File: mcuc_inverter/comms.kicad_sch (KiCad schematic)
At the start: 0 parts

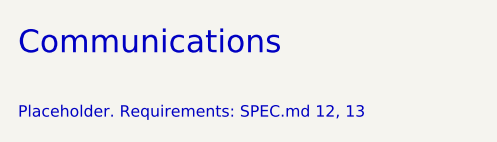
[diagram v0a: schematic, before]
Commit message: Design the supervisor interlock block
Adds docs/supervisor.md: the full logic design for the firmware-independent
hardware interlocks required by SPEC.md §9.2 -- overcurrent detect and latch,
fault aggregation, PWM overlap elimination and dead time. Includes the
24-signal interface, gate budget, and a failure-mode review done on the
assumption that firmware is hostile.

Two selections differ from the original PALTA board, both deliberate:

- Comparators run from +5 V, not 3.3 V. The LM2903's input common-mode
  ceiling is VCC-1.5V, so on 3.3 V it is 1.8 V -- below the 3.05 V positive
  trip point. The positive-overcurrent channel would never have asserted.
  Open-drain outputs still pull up to 3.3 V, so no level shifting is needed.
- 74HC replaces 74ACT. The dead-time RC assumes a CMOS threshold at
  0.5*VCC; 74ACT's TTL thresholds make the delay supply- and part-dependent.
  Predictable dead time beats ~10 ns of propagation delay here.

Adds tools/gen_skeleton.py, which generates the KiCad skeleton and records
the block interfaces, and ERC severities in mcuc_inverter.kicad_pro:
hier_label_mismatch stays an error, label_dangling and pin_not_connected
become warnings during build-out.

The interface is not emitted into the schematic yet (EMIT_INTERFACE=False).
Emitting it into empty sheets produces 96 legitimate dangling-label
violations, and copperhead check fails on warnings as well as errors, which
would leave the verification gate permanently red -- the same failure mode
that let the earlier generated documents through unchecked. The interface
lands in the same change as the components. Rationale in supervisor.md §9.

Verified: kicad-cli sch erc reports 0 violations and copperhead check is
green. With the interface temporarily emitted, ERC reported no
hier_label_mismatch, confirming all 24 names and directions agree across
every sheet boundary.

Co-Authored-By: Claude Opus 5 <noreply@anthropic.com>
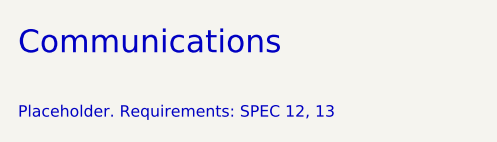
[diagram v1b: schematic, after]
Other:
- note added: "Placeholder. Requirements: SPEC 12, 13"
- note removed: "Placeholder. Requirements: SPEC.md 12, 13"
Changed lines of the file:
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@@
 		)
 	)
-	(text "Placeholder. Requirements: SPEC.md 12, 13"
+	(text "Placeholder. Requirements: SPEC 12, 13"
 		(exclude_from_sim no)
 		(at 20 27 0)
